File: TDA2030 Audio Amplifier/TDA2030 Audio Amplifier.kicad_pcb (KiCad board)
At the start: 2 copper layers, 46 x 45 mm, 19 parts, among them J1 8Ohm Speaker, J2 INPUT, U1 TDA2030

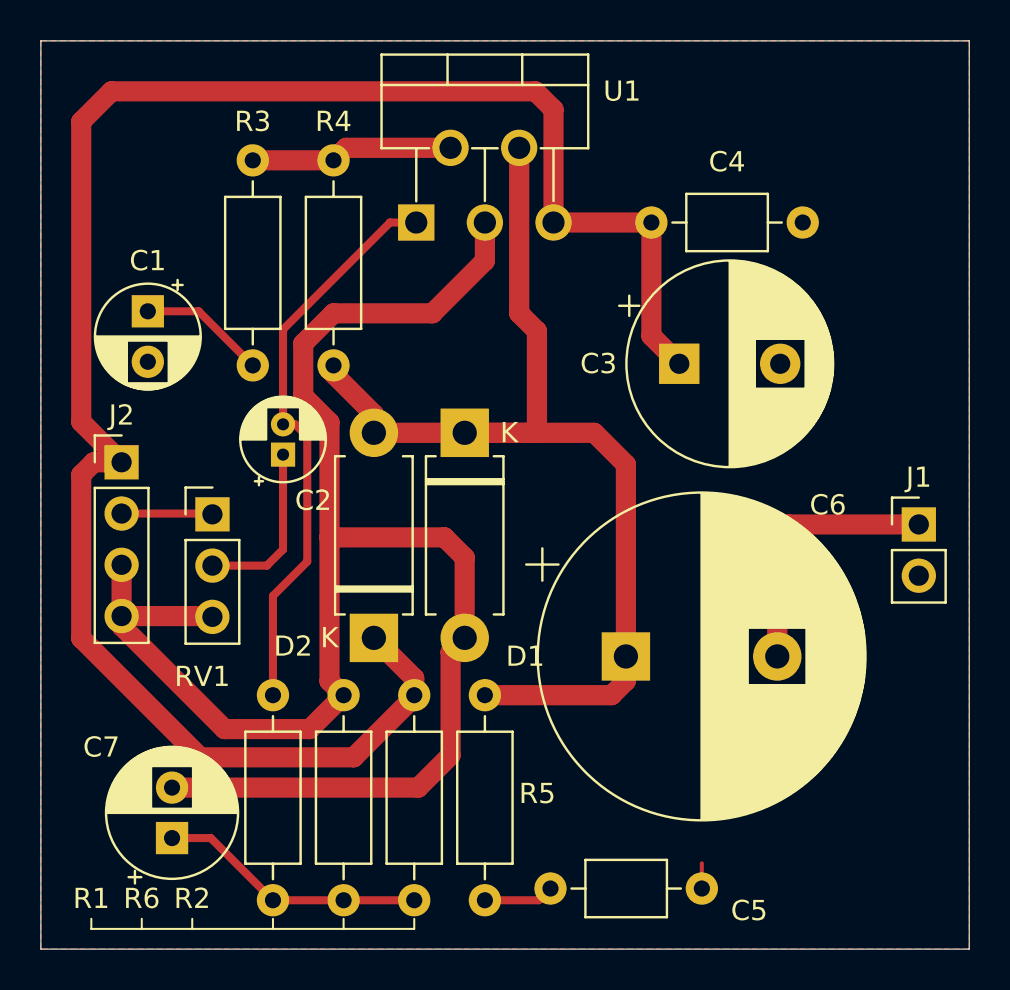
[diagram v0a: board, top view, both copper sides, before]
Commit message: Updated Vcc tracks.
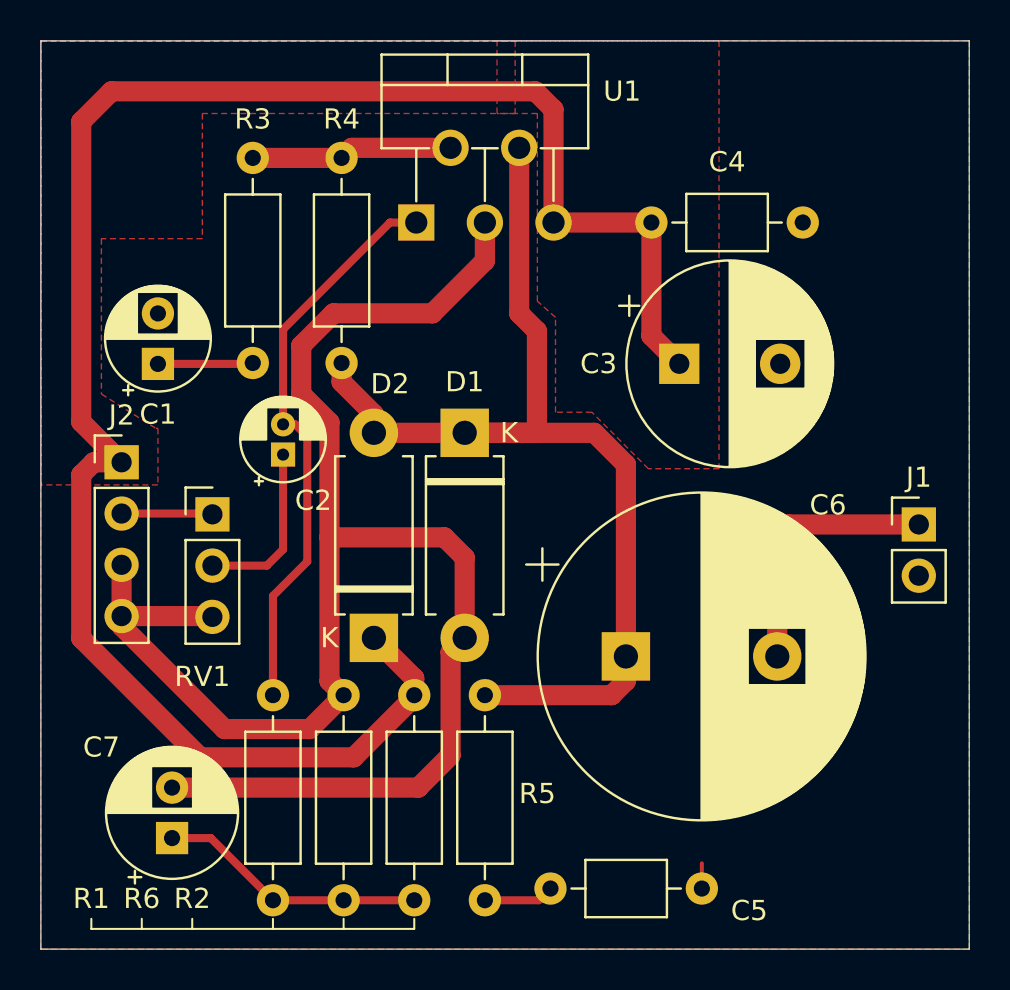
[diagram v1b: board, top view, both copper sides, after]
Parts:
- moved C1 2.65 mm to (105.8, 116.0), turned to 90 degrees
- moved R4 0.42 mm to (114.9, 105.8)
- moved R3 0.12 mm to (110.5, 105.8)
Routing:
- net Net-(C1-Pad1): track 6.45 -> 4.73 mm
- added copper zone on F.Cu, net VCC
